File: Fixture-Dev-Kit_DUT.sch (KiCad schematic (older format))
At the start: 31 parts, among them J5? CHIP4LH, J6? CHIP4RH, J8? CHIP4B2B

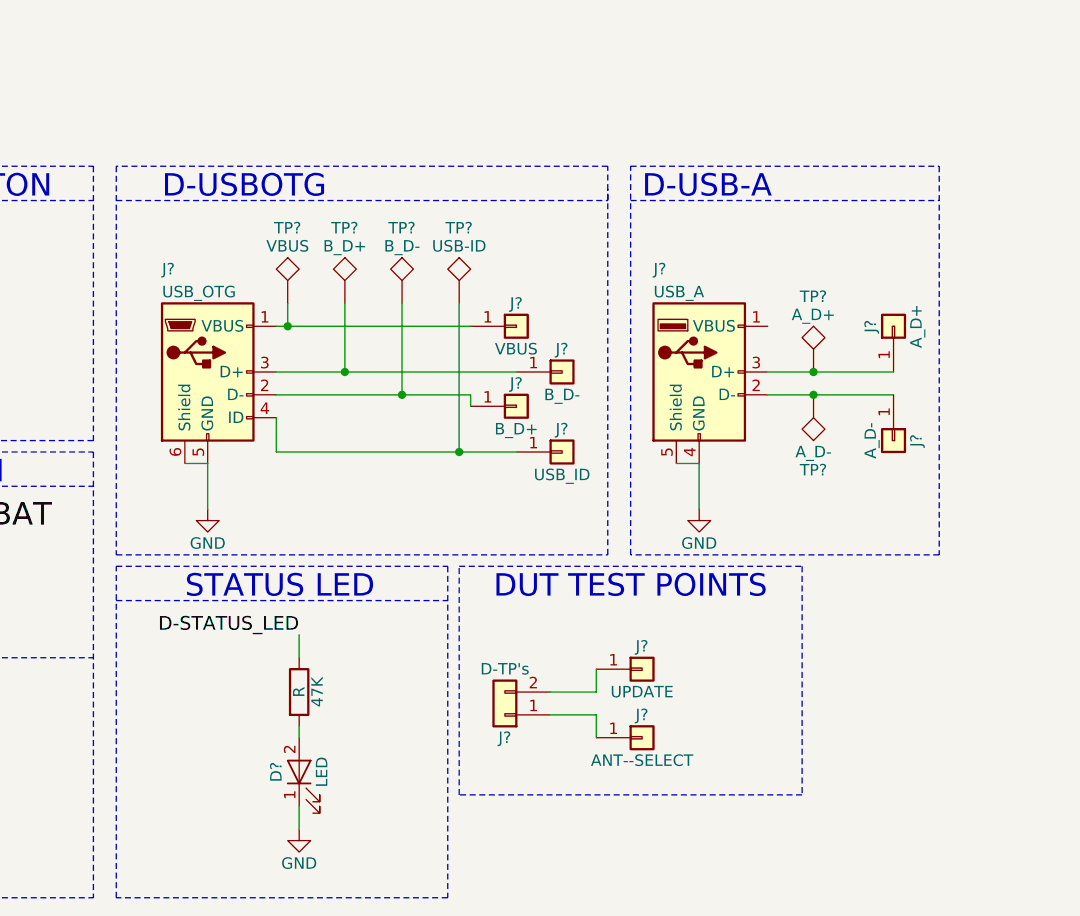
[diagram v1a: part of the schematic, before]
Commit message: adding LED and Button circuit
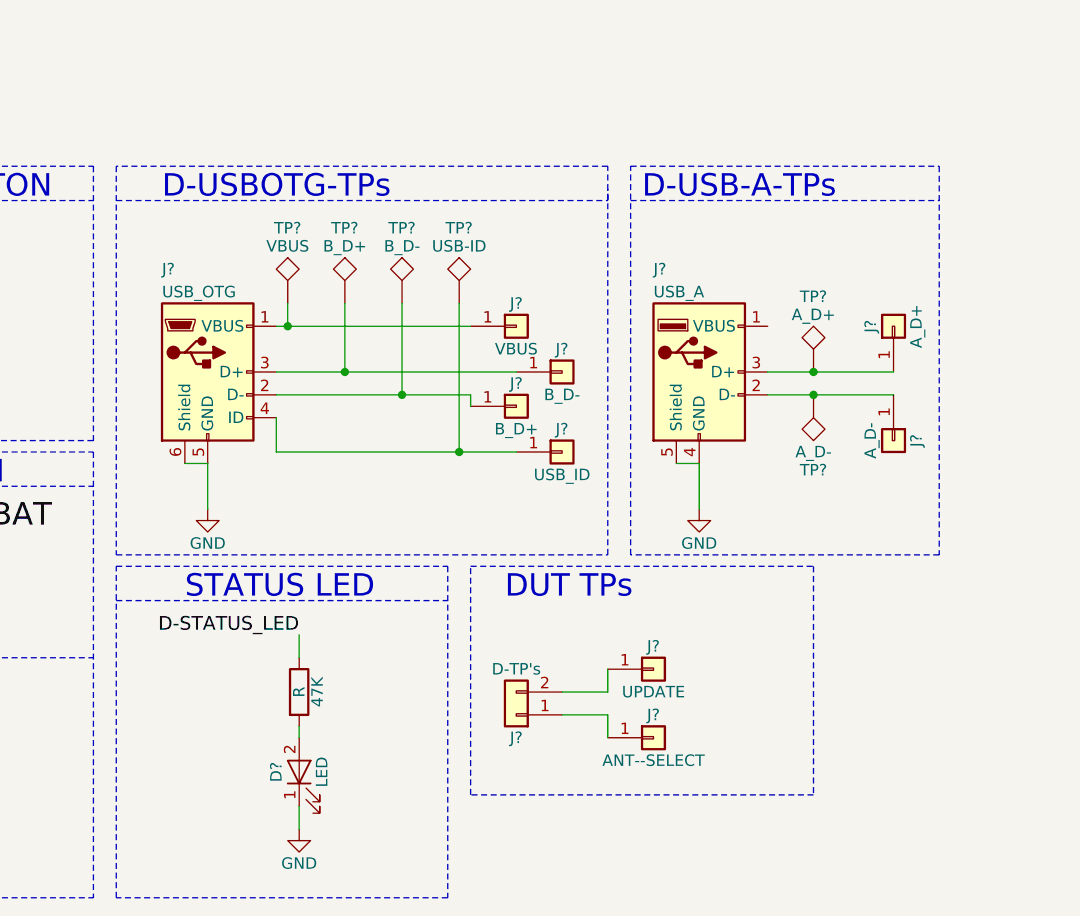
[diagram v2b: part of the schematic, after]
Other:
- note added: "D-USB-A-TPs\n"
- note added: "D-USBOTG-TPs\n"
- note added: "DUT TPs"
- note removed: "D-USB-A\n"
- note removed: "D-USBOTG"
- note removed: "DUT TEST POINTS"
- moved on the sheet: J?
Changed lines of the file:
@@
 $Descr A4 11693 8268
 encoding utf-8
-Sheet 2 6
+Sheet 2 7
 Title ""
 Date ""
@@
 Connection ~ 3600 5800
 Text Notes 2300 4700 0    98   ~ 0
-D-USBOTG
+D-USBOTG-TPs\n
 Wire Notes Line
 	2100 4550 2100 6250
@@
 	4650 5850 4650 6050
 Text Notes 4400 4700 0    98   ~ 0
-D-USB-A\n
+D-USB-A-TPs\n
 Wire Notes Line
 	4350 4550 5700 4550
@@
 L Conn_01x01 J?
 U 1 1 59EEA0FF
-P 4400 6750
-F 0 "J?" H 4400 6850 50  0000 C CNN
-F 1 "UPDATE" H 4400 6650 50  0000 C CNN
-F 2 "" H 4400 6750 50  0001 C CNN
-F 3 "" H 4400 6750 50  0001 C CNN
-	1    4400 6750
+P 4450 6750
+F 0 "J?" H 4450 6850 50  0000 C CNN
+F 1 "UPDATE" H 4450 6650 50  0000 C CNN
+F 2 "" H 4450 6750 50  0001 C CNN
+F 3 "" H 4450 6750 50  0001 C CNN
+	1    4450 6750
 	1    0    0    -1
 $EndComp
@@
 L Conn_01x01 J?
 U 1 1 59EEA2FD
-P 4400 7050
-F 0 "J?" H 4400 7150 50  0000 C CNN
-F 1 "ANT--SELECT" H 4400 6950 50  0000 C CNN
-F 2 "" H 4400 7050 50  0001 C CNN
-F 3 "" H 4400 7050 50  0001 C CNN
-	1    4400 7050
+P 4450 7050
+F 0 "J?" H 4450 7150 50  0000 C CNN
+F 1 "ANT--SELECT" H 4450 6950 50  0000 C CNN
+F 2 "" H 4450 7050 50  0001 C CNN
+F 3 "" H 4450 7050 50  0001 C CNN
+	1    4450 7050
 	1    0    0    -1
 $EndComp
@@
 L Conn_01x02 J?
 U 1 1 59EEA72D
-P 3800 6950
-F 0 "J?" H 3800 7050 50  0000 C CNN
-F 1 "D-TP's" H 3800 6750 50  0000 C CNN
-F 2 "" H 3800 6950 50  0001 C CNN
-F 3 "" H 3800 6950 50  0001 C CNN
-	1    3800 6950
+P 3850 6950
+F 0 "J?" H 3850 7050 50  0000 C CNN
+F 1 "D-TP's" H 3850 6750 50  0000 C CNN
+F 2 "" H 3850 6950 50  0001 C CNN
+F 3 "" H 3850 6950 50  0001 C CNN
+	1    3850 6950
 	-1   0    0    1
 $EndComp
 Wire Wire Line
-	4000 6850 4200 6850
-Wire Wire Line
-	4200 6850 4200 6750
-Wire Wire Line
-	4000 6950 4200 6950
-Wire Wire Line
-	4200 6950 4200 7050
-Text Notes 3750 6450 0    98   ~ 0
-DUT TEST POINTS
-Wire Notes Line
-	3600 6300 5100 6300
-Wire Notes Line
-	5100 6300 5100 7300
-Wire Notes Line
-	5100 7300 3600 7300
-Wire Notes Line
-	3600 7300 3600 6300
+	4050 6850 4250 6850
+Wire Wire Line
+	4250 6850 4250 6750
+Wire Wire Line
+	4050 6950 4250 6950
+Wire Wire Line
+	4250 6950 4250 7050
+Text Notes 3800 6450 0    98   ~ 0
+DUT TPs
+Wire Notes Line
+	3650 6300 5150 6300
+Wire Notes Line
+	5150 6300 5150 7300
+Wire Notes Line
+	5150 7300 3650 7300
+Wire Notes Line
+	3650 7300 3650 6300
 $EndSCHEMATC
